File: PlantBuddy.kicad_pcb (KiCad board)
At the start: 4 copper layers, 44.3 x 29.2 mm, 77 parts, among them J1 USB_C_Receptacle_USB2.0, J101 JST, J102 Debug, J4 External, SW1 SW_Push, U1 LTR-303ALS-01, U101 AP2139AK-3.0TRG1, U102 nRF52832-QFAA, U104 XB5350A, U105 CN809T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

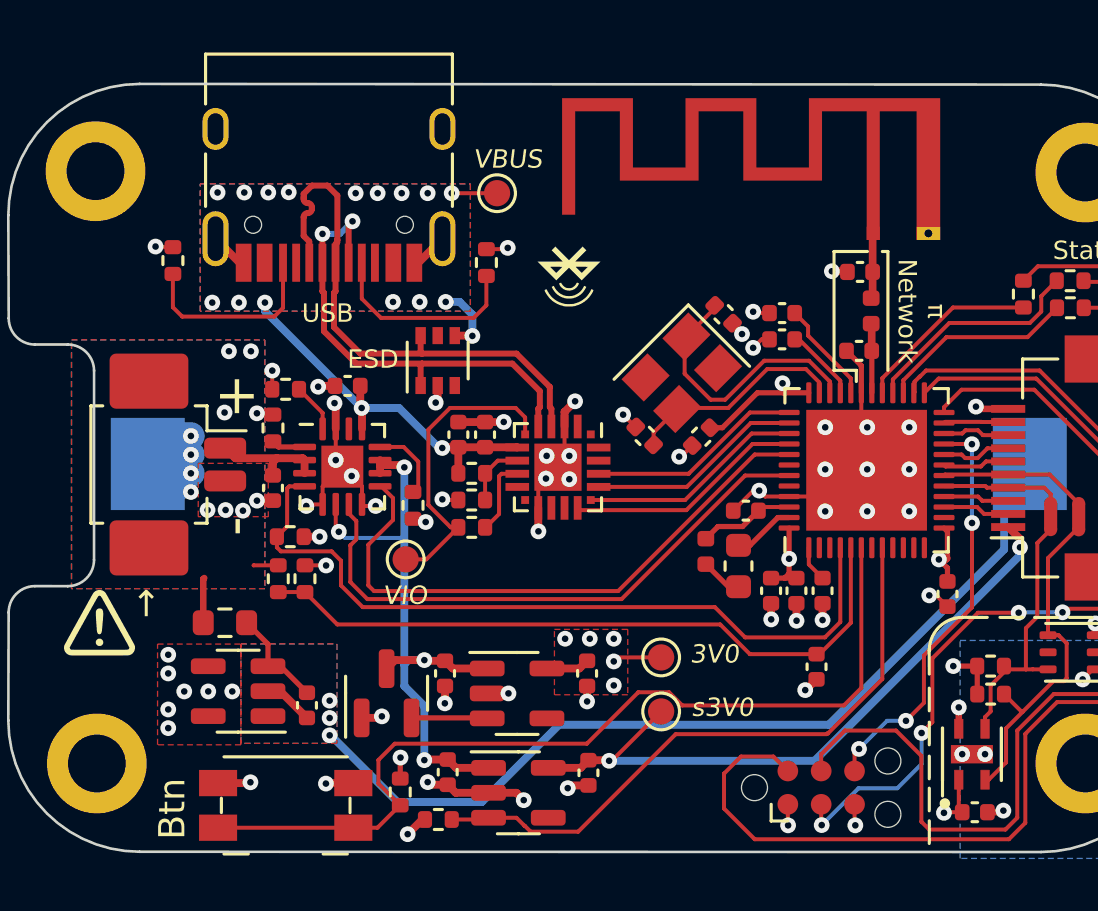
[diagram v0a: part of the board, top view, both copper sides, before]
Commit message: Changed antenna to 1.6mm-compatible one
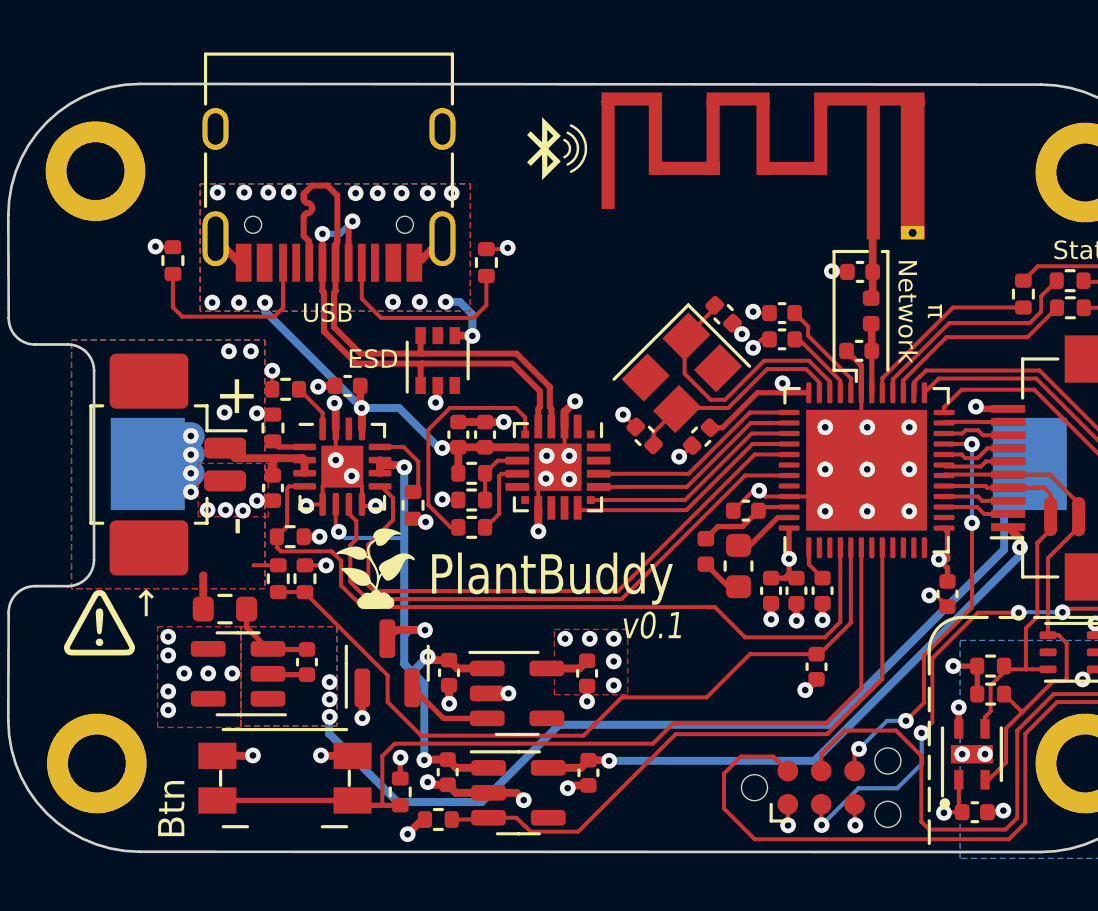
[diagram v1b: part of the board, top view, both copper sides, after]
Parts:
- removed TP101: TP_3V0, TestPoint:TestPoint_Pad_D1.0mm
- removed TP102: TP_s3V0, TestPoint:TestPoint_Pad_D1.0mm
- removed TP103: TP_VIN, TestPoint:TestPoint_Pad_D1.0mm
- removed TP104: TP_VIO, TestPoint:TestPoint_Pad_D1.0mm
- added G***: LOGO, LOGO, F.Cu at (129.8, 131.3)
- AE101: footprint RF_Antenna:Texas_SWRA117D_2.4GHz_Left -> wch-antenna:ANT-F-1-2.4G-1.6MM-FR4-WCH
- moved AE101 4.94 mm to (144.6, 115.8)
- moved G*** 4.81 mm to (136.6, 115.3), turned to 0 degrees
- moved C104 1.65 mm to (127.2, 134.8)
- moved U105 1.14 mm to (130.2, 134.9)
- moved SW1 1.04 mm to (126.3, 139.2)
- moved U104 0.66 mm to (124.6, 135.3)
- moved R103 0.52 mm to (124.1, 132.8)
- moved C10 0.15 mm to (132.6, 135.2)
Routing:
- net /batsense: track 26.1 -> 29.3 mm
- net /S_3V0: track 25.4 -> 22.6 mm
- net /V_IO: track 11.7 -> 9.19 mm
- net +3V0: track 21.9 -> 20.0 mm
- net VBUS: track 19.2 -> 17.5 mm
- net /btn: track 34.6 -> 33.7 mm
- net VCC: track 24.1 -> 24.9 mm, vias 4 -> 5
- net GND: track 56.4 -> 57.0 mm
- net /Bat_n: track 36.0 -> 36.6 mm
- net Net-(C104-Pad1): track 3.90 -> 3.35 mm
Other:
- board text added: "PlantBuddy"
- board text added: "v0.1"
- board text removed: "3V0"
- board text removed: "VBUS"
- board text removed: "VIO"
- board text removed: "s3V0"

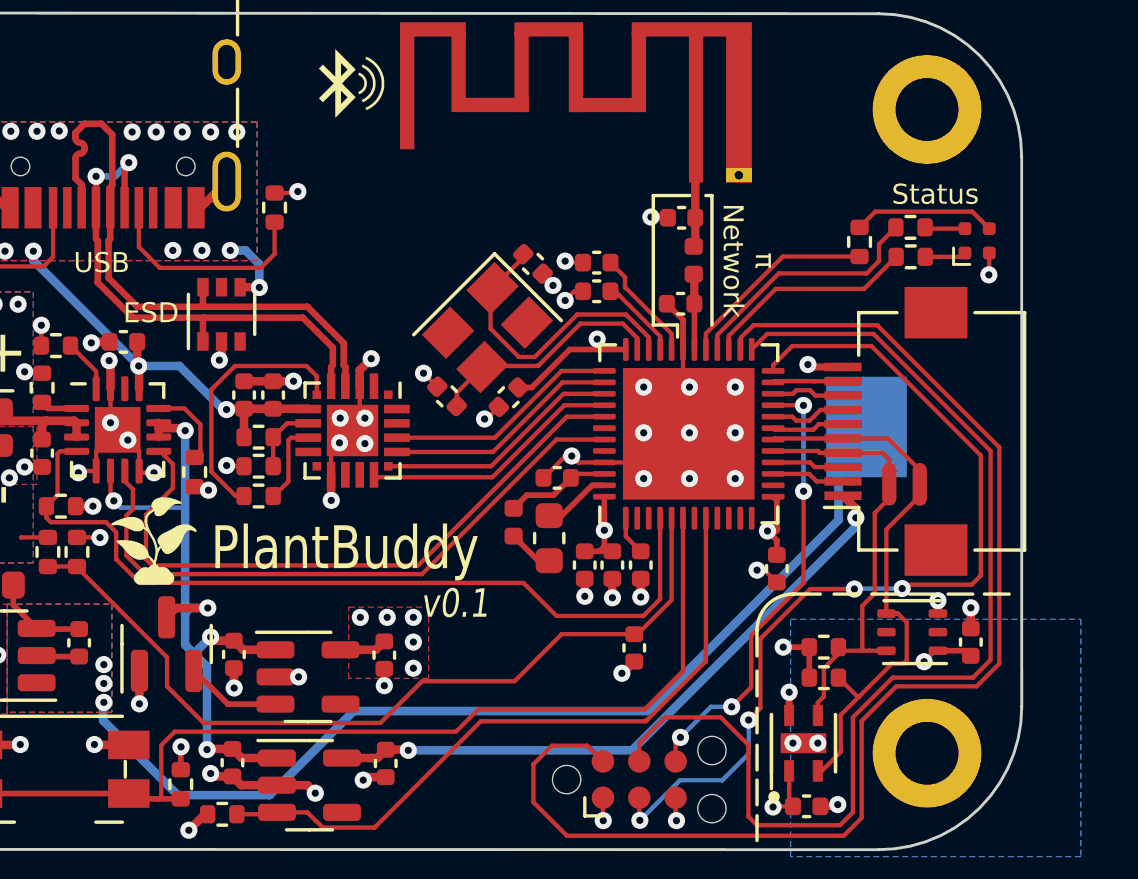
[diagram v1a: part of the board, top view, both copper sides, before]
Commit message: Corrected LED pins
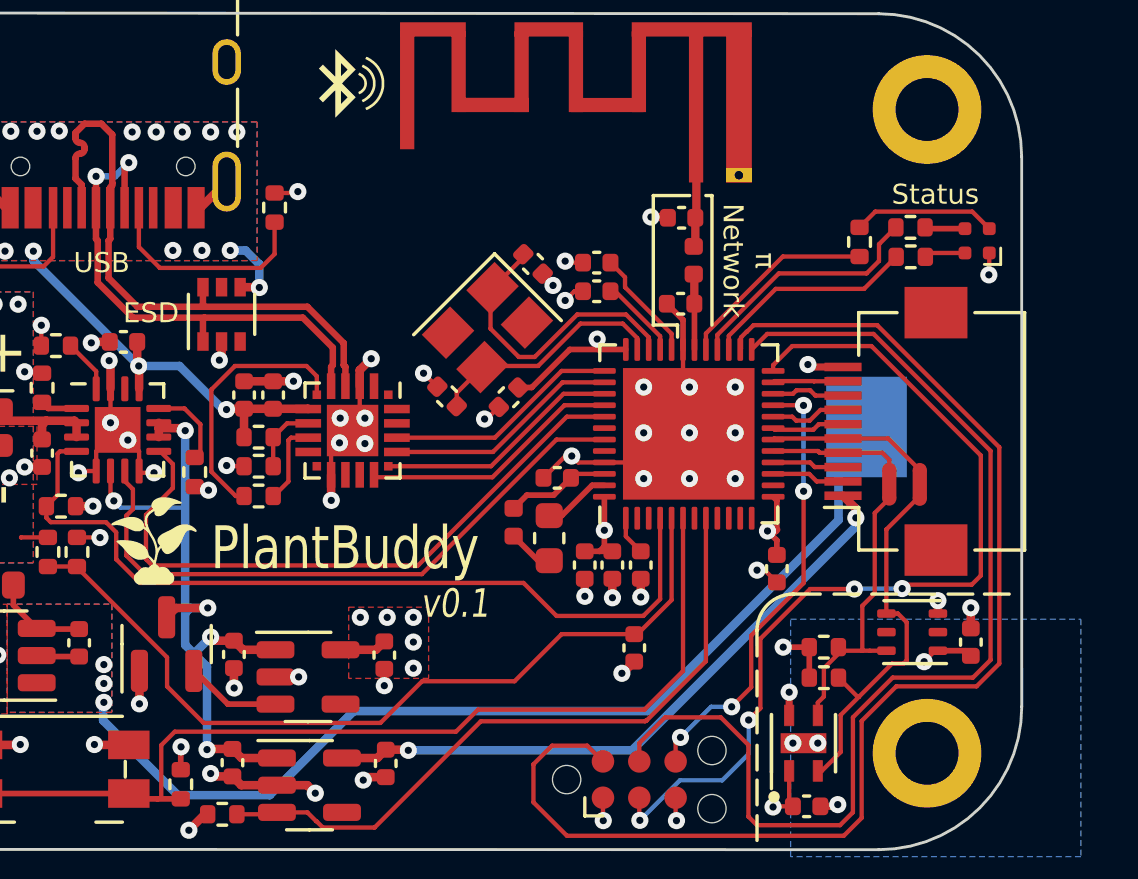
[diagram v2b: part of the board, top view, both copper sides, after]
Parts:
- turned D102 to 180 degrees
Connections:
- D102 pad 1: Net-(D102-Pad1) -> +3V0
- D102 pad 4: +3V0 -> Net-(D102-Pad4)
- R102 pad 1: Net-(D102-Pad1) -> Net-(D102-Pad2)
- R107 pad 1: Net-(D102-Pad3) -> Net-(D102-Pad4)
- R109 pad 1: Net-(D102-Pad2) -> Net-(D102-Pad3)
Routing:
- net Net-(D102-Pad4): track 0.00 -> 5.01 mm
- net Net-(D102-Pad3): track 5.01 -> 1.41 mm
- net Net-(D102-Pad1): track 1.44 -> 0.00 mm

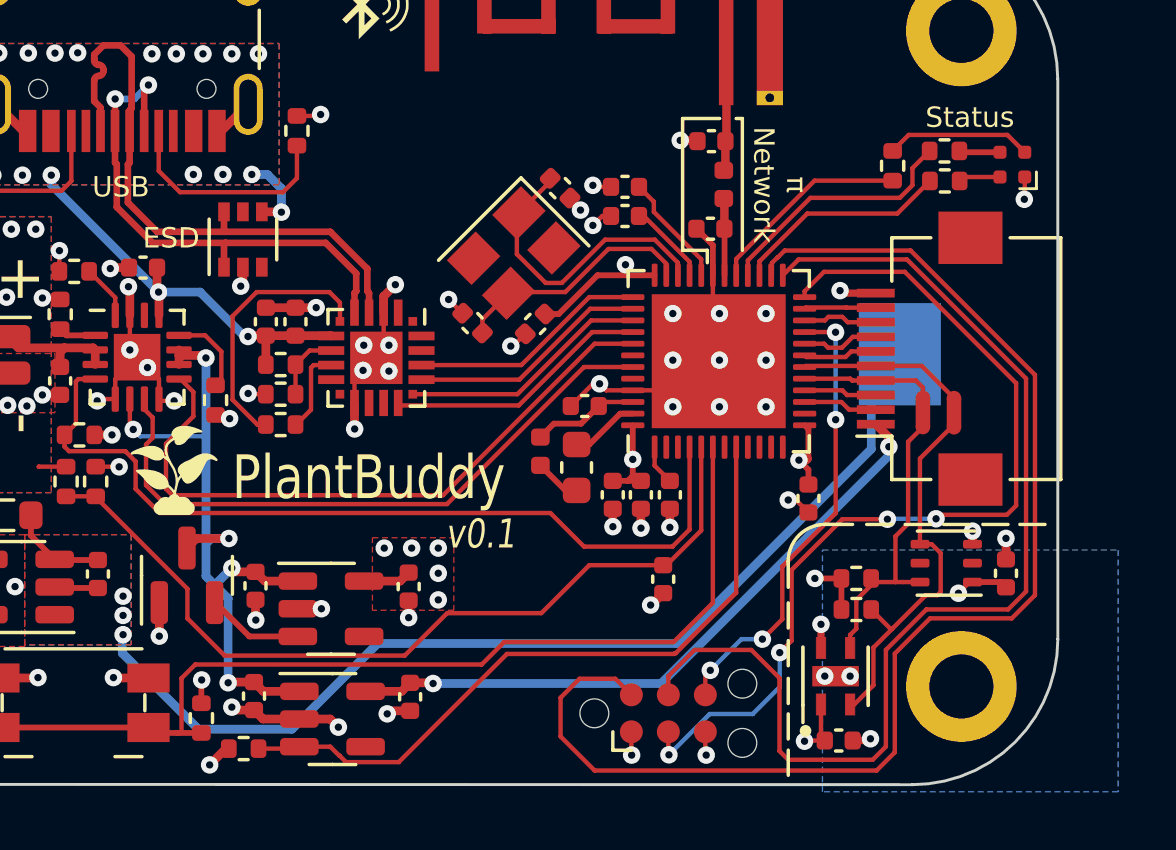
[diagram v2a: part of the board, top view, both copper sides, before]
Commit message: Connected button to reset pin
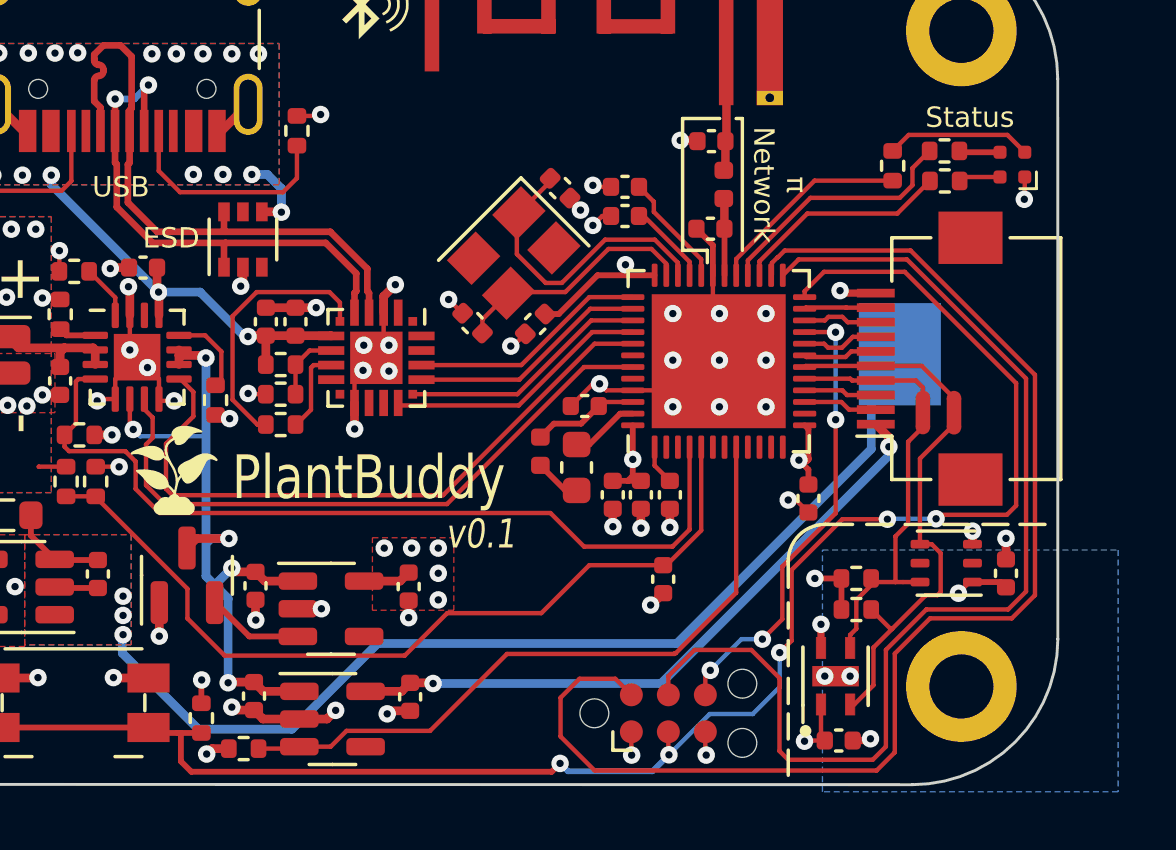
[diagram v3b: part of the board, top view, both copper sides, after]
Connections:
- R108 pad 1: /btn -> /~{tRST}
- SW1 pad 1: /btn -> /~{tRST}
- U102 pad 6: /btn -> unconnected-(U102-Pad6)
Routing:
- net /btn: track 33.7 -> 0.00 mm
- net /~{tRST}: track 31.9 -> 57.3 mm, vias 4 -> 5
